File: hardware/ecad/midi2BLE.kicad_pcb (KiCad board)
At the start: 2 copper layers, 100 x 30 mm, 18 parts, among them J1 Conn_01x02, U1 TPS62162DSG, U2 BQ24079RGTT

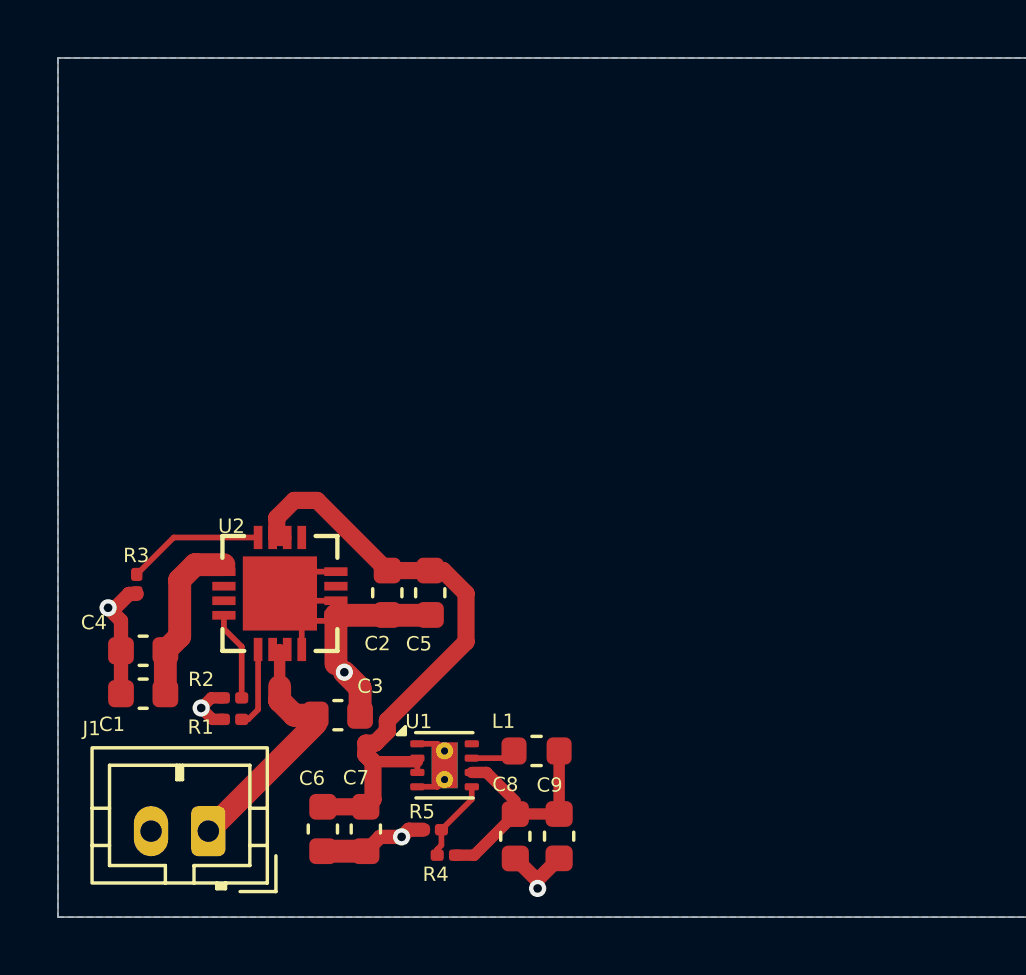
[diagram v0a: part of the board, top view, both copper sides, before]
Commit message: Power schematic finished, top level schematic editied to swap from I2c to SPI instead
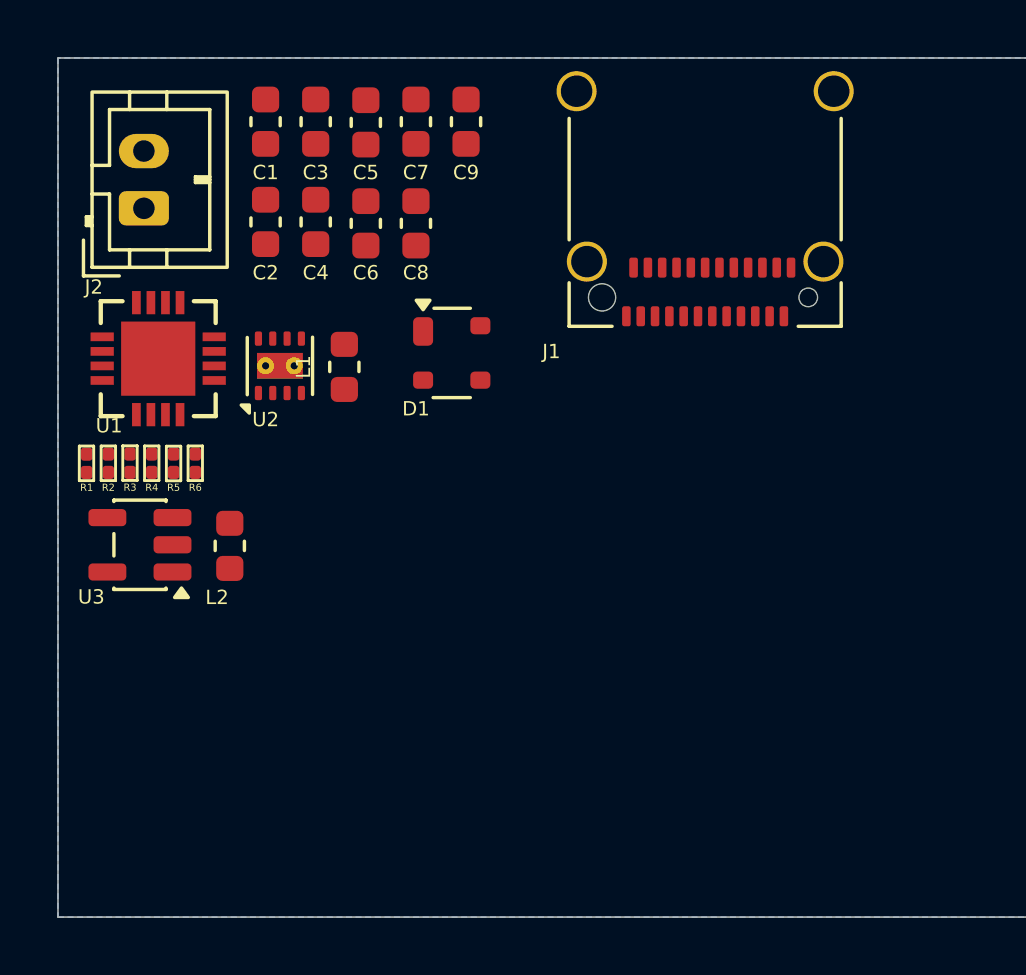
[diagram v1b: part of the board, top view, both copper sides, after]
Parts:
- added D1: PRTR5V0U2X, Package_TO_SOT_SMD:SOT-143, F.Cu at (104.2, 90.3)
- added J2: Conn_01x02, Connector_JST:JST_PH_B2B-PH-K_1x02_P2.00mm_Vertical, F.Cu at (93.5, 85.2)
- added L2: 2.2uH, Inductor_SMD:L_0603_1608Metric, F.Cu at (96.5, 97.0)
- added R6: 10k, Resistor_SMD:R_0201_0603Metric, F.Cu at (95.3, 94.2)
- added U3: TLV61047DDC, Package_TO_SOT_SMD:SOT-23-5, F.Cu at (93.4, 97.0)
- C4: value 0.1uF -> 10uF
- C5, C7, C9: value 0.1uF -> 100nF
- C6: value 10uF -> 100nF
- C8: value 22uF -> 100nF
- J1: value Conn_01x02 -> USB_C_Receptacle; footprint Connector_JST:JST_PH_B2B-PH-K_1x02_P2.00mm_Vertical -> Connector_USB:USB_C_Receptacle_Amphenol_12401610E4-2A_CircularHoles
- R1: value 10k -> 5.1k
- R2: value 2k -> 5.1k
- R3: value 1k -> 590
- R4: value 560k -> 1k
- R5: value 180k -> 10k
- U1: value TPS62162DSG -> BQ24079RGTT; footprint Package_SON:WSON-8-1EP_2x2mm_P0.5mm_EP0.9x1.6mm_ThermalVias -> footprints:QFN50P400X400X80-17N
- U2: value BQ24079RGTT -> TPS62162DSG; footprint footprints:QFN50P400X400X80-17N -> Package_SON:WSON-8-1EP_2x2mm_P0.5mm_EP0.9x1.6mm_ThermalVias
- moved J1 28.8 mm to (113.1, 84.0)
- moved C9 25.2 mm to (104.8, 82.2)
- moved C7 24.8 mm to (103.0, 82.2)
- moved C8 21.7 mm to (103.0, 85.8)
- moved C6 21.2 mm to (101.2, 85.8)
- moved C3 20.7 mm to (99.5, 82.2), turned to -90 degrees
- moved C1 20.4 mm to (97.8, 82.2), turned to -90 degrees
- moved U1 17.4 mm to (94.0, 90.5)
- moved R4 17.1 mm to (93.8, 94.2), turned to 90 degrees
- moved C5 16.6 mm to (101.2, 82.2)
- moved C4 16.1 mm to (99.5, 85.7), turned to -90 degrees
- moved R5 15.7 mm to (94.5, 94.2), turned to 90 degrees
- moved L1 15.0 mm to (100.5, 90.8), turned to 90 degrees
- moved C2 13.6 mm to (97.8, 85.7)
- moved R1 10.3 mm to (91.5, 94.2), turned to 90 degrees
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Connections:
- C1 pad 1: /Power/VBUS_IN -> GND
- C1 pad 2: /Power/GND -> /Power/VBUS_IN
- C2 pad 1: /Power/SYS_RAW -> GND
- C2 pad 2: /Power/GND -> /Power/J2 1 - U1 BAT_1
- C3 pad 1: /Power/BAT -> GND
- C3 pad 2: /Power/GND -> /Power/U2 FB - C3 P1
- C4 pad 1: /Power/VBUS_IN -> GND
- C4 pad 2: /Power/GND -> /Power/L2 P2 - C4 P1
- C5 pad 1: /Power/SYS_RAW -> GND
- C5 pad 2: /Power/GND -> /Power/VBUS_IN
- C6 pad 1: /Power/SYS_RAW -> GND
- C6 pad 2: /Power/GND -> /Power/U1 EN - U3 VIN
- C7 pad 1: /Power/SYS_RAW -> GND
- C7 pad 2: /Power/GND -> /Power/U2 FB - C3 P1
- C8 pad 1: /Power/SYS_3V3 -> GND
- C8 pad 2: /Power/GND -> /Power/L2 P2 - C4 P1
- C9 pad 1: /Power/SYS_3V3 -> GND
- C9 pad 2: /Power/GND -> /Power/L2 P2 - C5 P1
- L1 pad 1: Net-(U1-SW) -> /Power/U2 SW - L1 P1
- L1 pad 2: /Power/SYS_3V3 -> /Power/U2 FB - C3 P1
- R1 pad 1: /Power/GND -> GND
- R1 pad 2: Net-(U2-TS) -> /Power/J1 CC1 - R1 P1
- R2 pad 1: Net-(U2-ISET) -> GND
- R2 pad 2: /Power/GND -> /Power/J1 CC2 - R2 P1
- R3 pad 1: Net-(U2-ILIM) -> GND
- R3 pad 2: /Power/GND -> /Power/U1 ISET - R3 P1
- R4 pad 1: /Power/SYS_3V3 -> GND
- R4 pad 2: Net-(U1-FB) -> /Power/U1 ILIM - R4 P1
- R5 pad 1: /Power/GND -> GND
- R5 pad 2: Net-(U1-FB) -> /Power/VBUS_IN
- U1 pad 1: /Power/GND -> /Power/U1 TS - R6 P1
- U1 pad 2: /Power/SYS_RAW -> /Power/J2 1 - U1 BAT_1
- U1 pad 3: /Power/SYS_RAW -> /Power/J2 1 - U1 BAT_1
- U1 pad 4: /Power/GND -> GND
- U1 pad 5: Net-(U1-FB) -> /Power/VBUS_IN
- U1 pad 6: /Power/SYS_3V3 -> GND
- U1 pad 7: Net-(U1-SW) -> /Power/U2 PG - R7 P2
- U1 pad 8: unconnected-(U1-PG-Pad8) -> GND
- U1 pad 9: /Power/GND -> /Power/U1 ~CHG - R6 P2
- U2 pad 1: Net-(U2-TS) -> GND
- U2 pad 2: /Power/BAT -> /Power/U2 VIN - U1 OUT_1
- U2 pad 3: /Power/BAT -> /Power/U2 EN - U3 VIN
- U2 pad 4: /Power/GND -> GND
- U2 pad 5: /Power/GND -> /Power/U2 FB - C3 P1
- U2 pad 6: /Power/GND -> /Power/U2 FB - C3 P1
- U2 pad 7: unconnected-(U2-~{PGOOD}-Pad7) -> /Power/U2 SW - L1 P1
- U2 pad 8: /Power/GND -> /Power/U2 PG - R7 P2
- U2 pad 9: unconnected-(U2-~{CHG}-Pad9) -> GND
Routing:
- net /Power/GND: track 31.1 -> 0.00 mm, vias 5 -> 0
- net /Power/SYS_RAW: track 22.7 -> 0.00 mm
- net /Power/BAT: track 9.11 -> 0.00 mm
- net /Power/SYS_3V3: track 8.80 -> 0.00 mm
- net /Power/VBUS_IN: track 5.94 -> 0.00 mm
- net Net-(U2-ILIM): track 4.77 -> 0.00 mm
- net Net-(U2-ISET): track 3.14 -> 0.00 mm
- net Net-(U1-FB): track 2.89 -> 0.00 mm
- net Net-(U2-TS): track 2.81 -> 0.00 mm
- net Net-(U1-SW): track 1.58 -> 0.00 mm
- added copper zone on B.Cu, net /Power/U2 FB - C3 P1
- removed copper zone on B.Cu, net /Power/GND

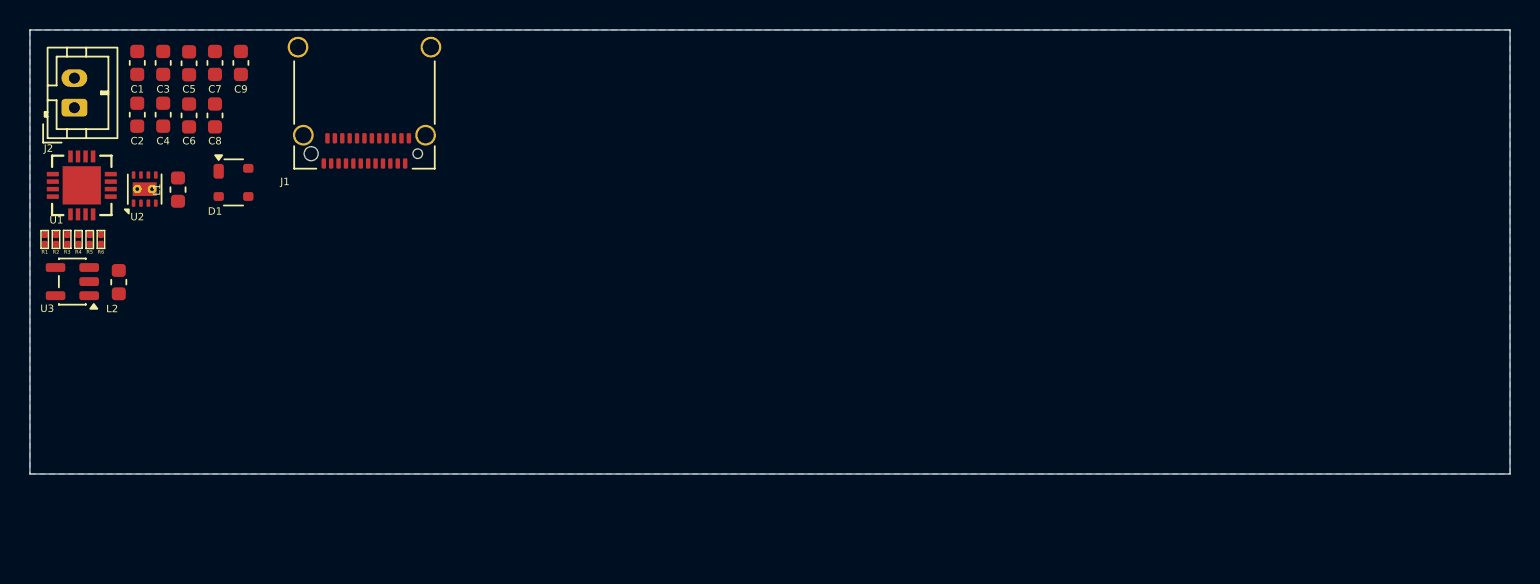
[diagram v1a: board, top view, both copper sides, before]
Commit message: finsihed 6/7 sheets, usb_data needs work. Some warnings to be dealt with aswell but no hard errors.
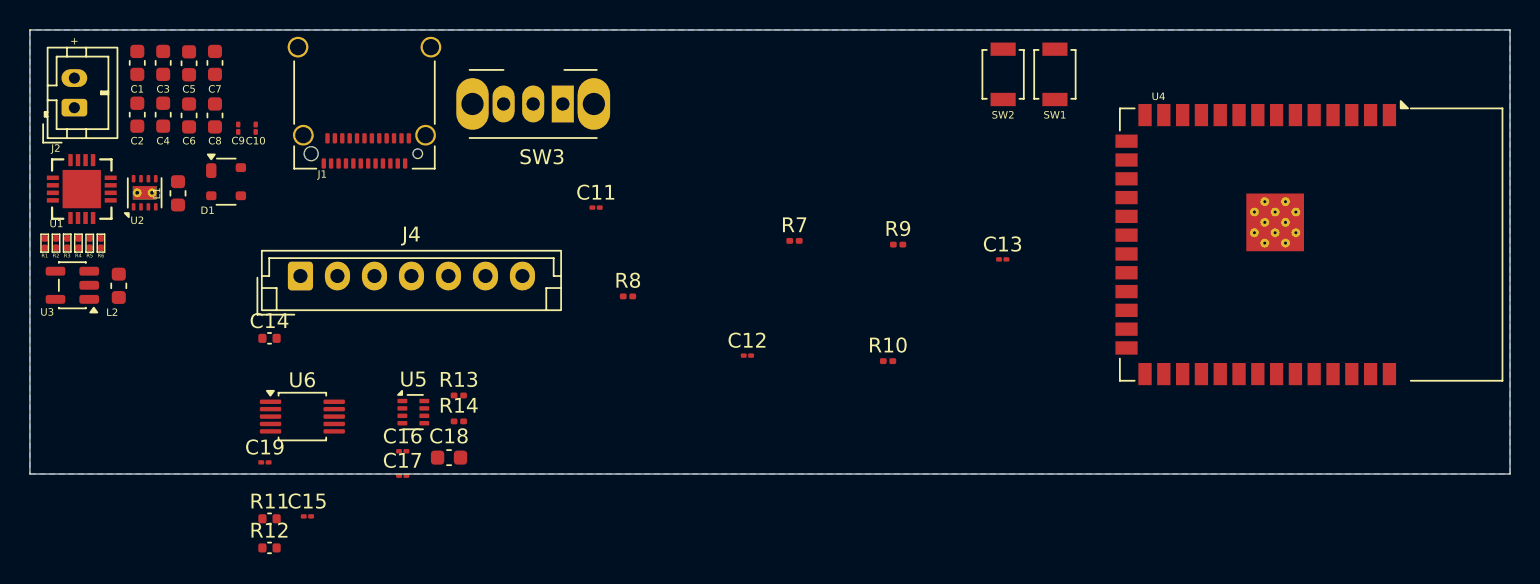
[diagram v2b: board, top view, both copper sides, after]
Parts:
- added C10: 10uF, Capacitor_SMD:C_01005_0402Metric, F.Cu at (105.8, 86.6)
- added C11: 100nF, Capacitor_SMD:C_01005_0402Metric, F.Cu at (128.8, 92.0)
- added C12: 100nF, Capacitor_SMD:C_01005_0402Metric, F.Cu at (139.0, 102.0)
- added C13: 100nF, Capacitor_SMD:C_01005_0402Metric, F.Cu at (156.2, 95.5)
- added C14: 100nF, Capacitor_SMD:C_0402_1005Metric, F.Cu at (106.7, 100.8)
- added C15: 100nF, Capacitor_SMD:C_01005_0402Metric, F.Cu at (109.2, 112.9)
- added C16: 100nF, Capacitor_SMD:C_01005_0402Metric, F.Cu at (115.7, 108.5)
- added C17: 100nF, Capacitor_SMD:C_01005_0402Metric, F.Cu at (115.7, 110.1)
- added C18: 10uF, Capacitor_SMD:C_0603_1608Metric, F.Cu at (118.8, 108.9)
- added C19: 100nF, Capacitor_SMD:C_01005_0402Metric, F.Cu at (106.4, 109.2)
- added J4: Conn_01x07, Connector_JST:JST_EH_B7B-EH-A_1x07_P2.50mm_Vertical, F.Cu at (108.8, 96.6)
- added R10: 100, Resistor_SMD:R_0201_0603Metric, F.Cu at (148.5, 102.4)
- added R11: 220k, Capacitor_SMD:C_0402_1005Metric, F.Cu at (106.7, 113.0)
- added R12: 100k, Capacitor_SMD:C_0402_1005Metric, F.Cu at (106.7, 115.0)
- added R13: 100k, Resistor_SMD:R_0201_0603Metric, F.Cu at (119.5, 104.7)
- added R14: 100k, Resistor_SMD:R_0201_0603Metric, F.Cu at (119.5, 106.4)
- added R7: 10k, Resistor_SMD:R_0201_0603Metric, F.Cu at (142.2, 94.2)
- added R8: 10k, Resistor_SMD:R_0201_0603Metric, F.Cu at (130.9, 98.0)
- added R9: 10k, Resistor_SMD:R_0201_0603Metric, F.Cu at (149.2, 94.5)
- added SW1: SW_Push, Button_Switch_SMD:SW_SPST_B3U-1000P, F.Cu at (159.8, 83.0)
- added SW2: SW_Push, Button_Switch_SMD:SW_SPST_B3U-1000P, F.Cu at (156.2, 83.0)
- added SW3: SW_SPDT, Button_Switch_THT:SW_Slide_SPDT_Angled_CK_OS102011MA1Q, F.Cu at (126.5, 85.0)
- added U4: ESP32-S3-WROOM-1, RF_Module:ESP32-S3-WROOM-1, F.Cu at (177.1, 94.5)
- added U5: TPS2116DRL, Package_TO_SOT_SMD:SOT-583-8, F.Cu at (116.4, 105.8)
- added U6: TS3USB30EDGSR, Package_SO:TSSOP-10_3x3mm_P0.5mm, F.Cu at (108.9, 106.1)
- C9: footprint Capacitor_SMD:C_0603_1608Metric -> Capacitor_SMD:C_01005_0402Metric
- moved C9 4.42 mm to (104.6, 86.6), turned to 90 degrees
- moved D1 0.50 mm to (103.8, 90.2)
- moved L1 0.25 mm to (100.5, 91.0)
- moved L2 0.25 mm to (96.5, 97.3)
- moved R1 0.25 mm to (91.5, 94.4)
- moved R2 0.25 mm to (92.3, 94.4)
- moved R3 0.25 mm to (93.0, 94.4)
- moved R4 0.25 mm to (93.8, 94.4)
- moved R5 0.25 mm to (94.5, 94.4)
- moved R6 0.25 mm to (95.3, 94.4)
- moved U1 0.25 mm to (94.0, 90.8)
- moved U2 0.25 mm to (98.2, 91.0)
- moved U3 0.25 mm to (93.4, 97.2)
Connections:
- C9 pad 1: GND -> /ESP32_S3/SYS_3V3
- C9 pad 2: /Power/L2 P2 - C5 P1 -> GND
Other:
- board text added: "+"

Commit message: feat: complete schematic design for midi2BLE v1
- Add 7-sheet hierarchical schematic covering full system architecture
- Power sheet: BQ24079RGTT charger, TPS62162DSG 3.3V buck, TLV61047DDC
  5V boost, PRTR5V0U2X ESD protection, USB-C receptacle with CC resistors
- ESP32-S3 sheet: WROOM-1-N8R2 module, UART header, boot/reset buttons,
  MODE_SEL debounce circuit, BAT_SENSE ADC input
- OLED UI sheet: SPI SSD1306 connector (GPIO35/36/10/9/8)
- Battery sense sheet: resistor divider for ADC1 battery voltage monitoring
- VBUS switching sheet: TPS2116DRL power mux for BOOST_5V/VBUS_IN selection
- USB data sheet: TS3USB30EDGSR USB 2.0 mux, keyboard USB-B connector,
  PRTR5V0U2X ESD protection on keyboard data lines
- Fix OLED from I2C to SPI, reassign GPIO11/12 away from octal flash
- Fix BQ24079 TS pin from VBUS_IN to 10k resistor to GND
- Set ISET=590R (1.5A charge), ILIM=1k (1.55A input limit) for 2500-3000mAh LiPo
- Pass ERC with 0 errors, 0 warnings (6 ignored: BQ24079 symbol quirks)
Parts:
- added D2: PRTR5V0U2X, Package_TO_SOT_SMD:SOT-143, F.Cu at (158.1, 105.4)
- added J6: Conn_01x04, Connector_JST:JST_PH_B4B-PH-K_1x04_P2.00mm_Vertical, F.Cu at (139.0, 85.2)
- U1: footprint footprints:QFN50P400X400X80-17N -> Package_DFN_QFN:VQFN-16-1EP_3x3mm_P0.5mm_EP1.68x1.68mm_ThermalVias
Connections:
- net /ESP32_S3/EN renamed /ESP32_S3/RST_BUTTON
- net /VBUS Switching/VBUS_KBD renamed VBUS_KBD
- C1 pad 2: /Power/VBUS_IN -> VBUS_IN
- C10 pad 1: /ESP32_S3/SYS_3V3 -> SYS_3V3
- C13 pad 2: /ESP32_S3/MODE_SEL -> MODE_SEL
- C14 pad 1: /OLED UI/SYS_3V3 -> SYS_3V3
- C14 pad 2: /OLED UI/GND -> GND
- C15 pad 1: /Battery Sense/BAT_SENSE -> BAT_SENSE
- C15 pad 2: /Battery Sense/GND -> GND
- C16 pad 1: /VBUS Switching/BOOST_5V -> BOOST_5V
- C16 pad 2: /VBUS Switching/GND -> GND
- C17 pad 1: /VBUS Switching/VBUS_IN -> VBUS_IN
- C17 pad 2: /VBUS Switching/GND -> GND
- C18 pad 2: /VBUS Switching/GND -> GND
- C19 pad 1: /USB Data/SYS_3V3 -> SYS_3V3
- C19 pad 2: /USB Data/GND -> GND
- C2 pad 2: /Power/J2 1 - U1 BAT_1 -> BAT
- C5 pad 2: /Power/VBUS_IN -> VBUS_IN
- C6 pad 2: /Power/U1 EN - U3 VIN -> /Power/U2 EN - U3 VIN
- C9 pad 1: /ESP32_S3/SYS_3V3 -> SYS_3V3
- D1 pad 2: /Power/J1 DP1 - J1 DP2 -> USB_D+_UP
- D1 pad 3: /Power/J1 DN1 - J1 DN2 -> USB_D-_UP
- D1 pad 4: /Power/VBUS_IN -> VBUS_IN
- J1 pad A4: /Power/VBUS_IN -> VBUS_IN
- J1 pad A6: /Power/J1 DP1 - J1 DP2 -> USB_D+_UP
- J1 pad A7: /Power/J1 DN1 - J1 DN2 -> USB_D-_UP
- J1 pad A8: /Power/J1 CC2 - R2 P1 -> unconnected-(J1-SBU1-PadA8)
- J1 pad A9: /Power/VBUS_IN -> VBUS_IN
- J1 pad B4: /Power/VBUS_IN -> VBUS_IN
- J1 pad B6: /Power/J1 DP1 - J1 DP2 -> USB_D+_UP
- J1 pad B7: /Power/J1 DN1 - J1 DN2 -> USB_D-_UP
- J1 pad B8: /Power/J1 CC2 - R2 P1 -> unconnected-(J1-SBU2-PadB8)
- J1 pad B9: /Power/VBUS_IN -> VBUS_IN
- J2 pad 2: /Power/J2 1 - U1 BAT_1 -> BAT
- J4 pad 1: /OLED UI/GND -> GND
- J4 pad 2: /OLED UI/SYS_3V3 -> SYS_3V3
- J4 pad 3: /OLED UI/OLED_CLK -> OLED_CLK
- J4 pad 4: /OLED UI/OLED_MOSI -> OLED_MOSI
- J4 pad 5: /OLED UI/OLED_RES -> OLED_RES
- J4 pad 6: /OLED UI/OLED_DC -> OLED_DC
- J4 pad 7: /OLED UI/OLED_CS -> OLED_CS
- R10 pad 1: /ESP32_S3/MODE_SEL -> MODE_SEL
- R11 pad 1: /Battery Sense/GND -> GND
- R11 pad 2: /Battery Sense/BAT_SENSE -> BAT_SENSE
- R12 pad 1: /Battery Sense/BAT_SENSE -> BAT_SENSE
- R12 pad 2: /Battery Sense/BAT -> BAT
- R13 pad 2: /VBUS Switching/BOOST_5V -> BOOST_5V
- R14 pad 2: /VBUS Switching/GND -> GND
- R5 pad 2: /Power/VBUS_IN -> VBUS_IN
- R7 pad 1: /ESP32_S3/SYS_3V3 -> SYS_3V3
- R8 pad 1: /ESP32_S3/SYS_3V3 -> SYS_3V3
- R9 pad 1: /ESP32_S3/MODE_SEL -> MODE_SEL
- SW3 pad 1: /ESP32_S3/SYS_3V3 -> SYS_3V3
- U1 pad 12: /Power/U1 ILIM - R2 P1 -> /Power/U1 ILIM - R4 P1
- U1 pad 13: /Power/J1 VBUS__1 - D1 VCC -> VBUS_IN
- U1 pad 2: /Power/J2 1 - U1 BAT_1 -> BAT
- U1 pad 3: /Power/J2 1 - U1 BAT_1 -> BAT
- U1 pad 5: /Power/VBUS_IN -> VBUS_IN
- U1 pad 9: /Power/U1 ~CHG - R6 P2 -> unconnected-(U1-~{CHG}-Pad9)
- U2 pad 2: /Power/U2 VIN - U1 OUT_1 -> /Power/U1 OUT_2 - U2 VIN
- U2 pad 5: /Power/U2 FB - C3 P1 -> SYS_3V3
- U3 pad 3: /Power/L2 P2 - C4 P1 -> BOOST_5V
- U4 pad 12: /ESP32_S3/OLED_RES -> OLED_RES
- U4 pad 13: /ESP32_S3/USB_D-_ESP -> USB_D-_ESP
- U4 pad 14: /ESP32_S3/USB_D+_ESP -> USB_D+_ESP
- U4 pad 17: /ESP32_S3/OLED_CS -> OLED_CS
- U4 pad 18: /ESP32_S3/OLED_DC -> OLED_DC
- U4 pad 2: /ESP32_S3/SYS_3V3 -> SYS_3V3
- U4 pad 28: /ESP32_S3/OLED_MOSI -> OLED_MOSI
- U4 pad 29: /ESP32_S3/OLED_CLK -> OLED_CLK
- U4 pad 38: /ESP32_S3/MODE_SEL -> MODE_SEL
- U4 pad 4: /ESP32_S3/BAT_SENSE -> BAT_SENSE
- U5 pad 1: /VBUS Switching/GND -> GND
- U5 pad 3: /VBUS Switching/BOOST_5V -> BOOST_5V
- U5 pad 5: /VBUS Switching/MODE_SEL -> MODE_SEL
- U5 pad 6: /VBUS Switching/VBUS_IN -> VBUS_IN
- U5 pad 8: /VBUS Switching/GND -> unconnected-(U5-ST-Pad8)
- U6 pad 1: unconnected-(U6-S-Pad1) -> MODE_SEL
- U6 pad 10: /USB Data/SYS_3V3 -> SYS_3V3
- U6 pad 2: /USB Data/USB_D+_ESP -> USB_D+_ESP
- U6 pad 3: /USB Data/USB_D+_UP -> USB_D+_UP
- U6 pad 4: /USB Data/USB_D+_KBD -> USB_D+_KBD
- U6 pad 5: /USB Data/GND -> GND
- U6 pad 6: /USB Data/USB_D-_KBD -> USB_D-_KBD
- U6 pad 7: /USB Data/USB_D-_UP -> USB_D-_UP
- U6 pad 8: /USB Data/USB_D-_ESP -> USB_D-_ESP
- U6 pad 9: /USB Data/MODE_SEL -> MODE_SEL
